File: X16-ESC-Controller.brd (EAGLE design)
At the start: 51.6 x 34.2 mm, 23 parts, among them J6 TMMH-110-05-F-D, U1 AZ1117IH-3.3TRG1

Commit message: 12/6/2023 pt2
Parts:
- renumbered JP1 to .., JP2 to .
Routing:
- net TIM1_CH2: track 46.4 -> 48.0 mm
- net GND: track 86.2 -> 84.9 mm
- net TIM3_CH2: track 49.6 -> 50.6 mm
- net TIM1_CH1: track 45.7 -> 46.3 mm
- net NRST: track 56.4 -> 57.0 mm
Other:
- board text added: "3V3"
- board text added: "NRST"
- board text added: "SWCLK"
- board text added: "SWDIO"

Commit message: 12/06/2023 pt3
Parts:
- D1, D2: device SparkFun-LED:LED-0603 -> SparkFun-LED:LED-0805
- moved D1 0.13 mm to (35.1, 27.6)
- moved D2 0.13 mm to (2.03, 9.14), turned to 270 degrees
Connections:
- removed net N$16: D2.A, R6.2
- new net N$1: D2.C, R6.2
- net 3V3: now also D2.A; no longer D2.C
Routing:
- net N$16: track 3.35 -> 0.00 mm
- net N$1: track 0.00 -> 3.31 mm
- net GND: track 84.9 -> 84.8 mm, vias 8 -> 26
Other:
- board text added: "5.2V"
- board text added: "Manya Kodi"
- board text added: "TIM1_CH1"
- board text added: "TIM1_CH2"
- board text added: "TIM1_CH3"
- board text added: "TIM1_CH4"
- board text added: "TIM2_CH1"
- board text added: "TIM2_CH2"
- board text added: "TIM2_CH3"
- board text added: "TIM2_CH4"
- board text added: "TIM3_CH1"
- board text added: "TIM3_CH2"
- board text added: "TIM3_CH3"
- board text added: "TIM3_CH4"
- board text added: "X16-ESC-CONTROLLER"
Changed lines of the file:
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@@
 <drawing>
 <settings>
-<setting alwaysvectorfont="no"/>
+<setting alwaysvectorfont="yes"/>
 <setting verticaltext="up"/>
 </settings>
@@
 <text x="46.609" y="29.337" size="0.508" layer="25">GND</text>
 <text x="46.482" y="32.004" size="0.508" layer="25">3V3</text>
+<text x="20.701" y="30.988" size="0.508" layer="25" rot="R90">TIM2_CH4</text>
+<text x="23.622" y="30.861" size="0.508" layer="25" rot="R90">TIM2_CH3</text>
+<text x="26.162" y="30.861" size="0.508" layer="25" rot="R90">TIM2_CH2</text>
+<text x="28.829" y="30.988" size="0.508" layer="25" rot="R90">TIM2_CH1</text>
+<text x="31.369" y="30.861" size="0.508" layer="25" rot="R90">TIM1_CH2</text>
+<text x="33.909" y="30.988" size="0.508" layer="25" rot="R90">TIM1_CH1</text>
+<text x="35.56" y="0.762" size="0.508" layer="25" rot="R90">TIM1_CH3</text>
+<text x="38.227" y="0.762" size="0.508" layer="25" rot="R90">TIM1_CH4</text>
+<text x="40.767" y="0.762" size="0.508" layer="25" rot="R90">TIM3_CH1</text>
+<text x="43.307" y="0.889" size="0.508" layer="25" rot="R90">TIM3_CH2</text>
+<text x="45.847" y="0.889" size="0.508" layer="25" rot="R90">TIM3_CH3</text>
+<text x="48.387" y="0.889" size="0.508" layer="25" rot="R90">TIM3_CH4</text>
+<text x="9.398" y="30.734" size="0.8128" layer="25" rot="R180">GND</text>
+<text x="9.144" y="23.368" size="0.8128" layer="25" rot="R180">3V3</text>
+<text x="13.208" y="3.302" size="0.8128" layer="25" rot="R180">5.2V</text>
+<text x="11.176" y="29.464" size="0.6096" layer="25">X16-ESC-CONTROLLER</text>
+<text x="11.938" y="28.321" size="0.6096" layer="25">Manya Kodi</text>
 </plain>
 <attributes>
@@
 <attribute name="VALUE" x="10.795" y="19.177" size="0.6096" layer="27" font="vector" ratio="20" rot="R90" align="top-center"/>
 </element>
-<element name="D1" library="SparkFun-LED" library_urn="urn:adsk.eagle:library:529" package="LED-0603" package3d_urn="urn:adsk.eagle:package:39354/2" value="Green" x="35.179" y="27.559" smashed="yes" rot="R180">
-<attribute name="NAME" x="35.179" y="26.924" size="0.6096" layer="25" font="vector" ratio="20" rot="R180" align="bottom-center"/>
-<attribute name="PROD_ID" value="DIO-16512" x="-10.541" y="74.549" size="1.778" layer="27" rot="R180" display="off"/>
-<attribute name="VALUE" x="35.179" y="28.194" size="0.6096" layer="27" font="vector" ratio="20" rot="R180" align="top-center"/>
-</element>
-<element name="D2" library="SparkFun-LED" library_urn="urn:adsk.eagle:library:529" package="LED-0603" package3d_urn="urn:adsk.eagle:package:39354/2" value="Green" x="2.032" y="9.017" smashed="yes" rot="R90">
-<attribute name="NAME" x="1.397" y="9.017" size="0.6096" layer="25" font="vector" ratio="20" rot="R90" align="bottom-center"/>
-<attribute name="PROD_ID" value="DIO-16512" x="49.022" y="58.547" size="1.778" layer="27" rot="R90" display="off"/>
-<attribute name="VALUE" x="2.667" y="9.017" size="0.6096" layer="27" font="vector" ratio="20" rot="R90" align="top-center"/>
+<element name="D1" library="SparkFun-LED" library_urn="urn:adsk.eagle:library:529" package="LED-0805" package3d_urn="urn:adsk.eagle:package:41389318/1" value="Green" x="35.052" y="27.559" smashed="yes" rot="R180">
+<attribute name="NAME" x="35.052" y="26.924" size="0.6096" layer="25" font="vector" ratio="20" rot="R180" align="bottom-center"/>
+</element>
+<element name="D2" library="SparkFun-LED" library_urn="urn:adsk.eagle:library:529" package="LED-0805" package3d_urn="urn:adsk.eagle:package:41389318/1" value="Green" x="2.032" y="9.144" smashed="yes" rot="R270">
+<attribute name="NAME" x="2.667" y="9.144" size="0.6096" layer="25" font="vector" ratio="20" rot="R270" align="bottom-center"/>
 </element>
 <element name="J1" library="SparkFun-Connectors" library_urn="urn:adsk.eagle:library:513" package="1X06_NO_SILK" package3d_urn="urn:adsk.eagle:package:38130/2" value="" x="34.798" y="32.385" smashed="yes" rot="R180">
@@
 <wire x1="33.528" y1="19.343" x2="31.242" y2="19.343" width="0.2032" layer="16"/>
 <wire x1="31.168" y1="22.544" x2="31.968" y2="22.544" width="0.2032" layer="1"/>
-<wire x1="31.968" y1="25.225" x2="34.302" y2="27.559" width="0.2032" layer="1"/>
-<wire x1="31.968" y1="22.544" x2="31.968" y2="25.225" width="0.2032" layer="1"/>
+<wire x1="31.968" y1="25.362165625" x2="34.002" y2="27.559" width="0.2032" layer="1"/>
+<wire x1="31.968" y1="22.544" x2="31.968" y2="25.362165625" width="0.2032" layer="1"/>
 <via x="31.877" y="17.907" extent="1-16" drill="0.35"/>
 <wire x1="35.648" y1="14.898" x2="36.576" y2="14.898" width="0.2032" layer="1"/>
@@
 <wire x1="43.561" y1="12.7" x2="43.942" y2="12.319" width="0.2032" layer="16"/>
 <wire x1="43.942" y1="12.319" x2="43.942" y2="6.985" width="0.2032" layer="16"/>
+<via x="9.398" y="32.004" extent="1-16" drill="0.35"/>
+<via x="4.826" y="15.367" extent="1-16" drill="0.35"/>
+<via x="4.953" y="11.43" extent="1-16" drill="0.35"/>
+<via x="4.953" y="7.239" extent="1-16" drill="0.35"/>
+<via x="12.446" y="13.843" extent="1-16" drill="0.35"/>
+<via x="12.446" y="10.16" extent="1-16" drill="0.35"/>
+<via x="12.573" y="6.35" extent="1-16" drill="0.35"/>
+<via x="9.652" y="28.702" extent="1-16" drill="0.35"/>
+<via x="9.652" y="25.019" extent="1-16" drill="0.35"/>
+<via x="14.351" y="25.019" extent="1-16" drill="0.35"/>
+<via x="18.669" y="25.019" extent="1-16" drill="0.35"/>
+<via x="38.227" y="32.004" extent="1-16" drill="0.35"/>
+<via x="41.656" y="32.004" extent="1-16" drill="0.35"/>
+<via x="45.212" y="32.004" extent="1-16" drill="0.35"/>
+<via x="45.466" y="27.686" extent="1-16" drill="0.35"/>
+<via x="43.561" y="30.099" extent="1-16" drill="0.35"/>
+<via x="30.099" y="26.543" extent="1-16" drill="0.35"/>
+<via x="46.609" y="20.193" extent="1-16" drill="0.35"/>
 </signal>
 <signal name="TIM2_CH1">
@@
 <wire x1="35.4076" y1="1.3716" x2="30.353" y2="1.3716" width="0.2032" layer="16"/>
 <wire x1="30.353" y1="1.3716" x2="29.819021875" y2="1.905578125" width="0.2032" layer="16"/>
-<wire x1="29.819021875" y1="3.532021875" x2="30.859" y2="4.572" width="0.2032" layer="16"/>
-<wire x1="29.819021875" y1="1.905578125" x2="29.819021875" y2="3.532021875" width="0.2032" layer="16"/>
+<wire x1="30.859" y1="4.191" x2="29.819021875" y2="3.151021875" width="0.2032" layer="16"/>
+<wire x1="30.859" y1="4.191" x2="30.859" y2="4.572" width="0.2032" layer="16"/>
+<wire x1="29.819021875" y1="1.905578125" x2="29.819021875" y2="3.151021875" width="0.2032" layer="16"/>
 <wire x1="40.8714" y1="7.62" x2="40.894" y2="7.6426" width="0.2032" layer="1"/>
 <wire x1="40.894" y1="16.891" x2="40.894" y2="7.6426" width="0.2032" layer="1"/>
@@
 <contactref element="R2" pad="2"/>
 <contactref element="D1" pad="A"/>
-<wire x1="36.056" y1="27.559" x2="36.056" y2="25.808" width="0.2032" layer="1"/>
-<wire x1="36.056" y1="25.808" x2="36.029" y2="25.781" width="0.2032" layer="1"/>
+<wire x1="36.029" y1="25.781" x2="36.029" y2="26.8201375" width="0.2032" layer="1"/>
+<wire x1="36.102" y1="27.559" x2="36.029" y2="26.8201375" width="0.2032" layer="1"/>
 </signal>
 <signal name="MISO">
@@
 <wire x1="18.859" y1="14.922" x2="18.859" y2="4.572" width="0.2032" layer="16"/>
 <wire x1="19.4338" y1="15.4968" x2="18.859" y2="14.922" width="0.2032" layer="16"/>
-</signal>
-<signal name="N$16">
-<contactref element="R6" pad="2"/>
-<contactref element="D2" pad="A"/>
-<wire x1="2.032" y1="8.14" x2="2.032" y2="4.787" width="0.2032" layer="1"/>
 </signal>
 <signal name="MOSI">
@@
 <contactref element="U1" pad="2"/>
 <contactref element="C7" pad="1"/>
-<contactref element="D2" pad="C"/>
 <wire x1="33.528" y1="21.043" x2="31.242" y2="21.043" width="0.508" layer="16"/>
 <wire x1="31.242" y1="21.043" x2="28.36" y2="21.043" width="0.508" layer="16"/>
@@
 <wire x1="4.318" y1="22.606" x2="4.064" y2="22.86" width="0.508" layer="1"/>
 <wire x1="4.318" y1="22.606" x2="4.318" y2="18.454" width="0.508" layer="1"/>
-<wire x1="2.032" y1="9.894" x2="2.032" y2="16.168" width="0.508" layer="1"/>
-<wire x1="2.032" y1="16.168" x2="4.191" y2="18.327" width="0.508" layer="1"/>
+<wire x1="2.032" y1="16.168" x2="2.1395" y2="16.2755" width="0.508" layer="1"/>
+<wire x1="2.0125" y1="16.1485" x2="2.032" y2="16.168" width="0.508" layer="1"/>
+<wire x1="2.1395" y1="16.2755" x2="4.191" y2="18.327" width="0.508" layer="1"/>
 <wire x1="4.191" y1="18.327" x2="4.318" y2="18.454" width="0.508" layer="1"/>
 <contactref element="R1" pad="2"/>
@@
 <wire x1="27.686" y1="20.447" x2="28.321" y2="21.082" width="0.508" layer="1"/>
 <wire x1="27.686" y1="20.447" x2="27.686" y2="18.288" width="0.508" layer="1"/>
+<contactref element="D2" pad="A"/>
+<wire x1="2.0125" y1="16.1485" x2="2.0125" y2="10.2135" width="0.508" layer="1"/>
+<wire x1="2.032" y1="10.194" x2="2.0125" y2="10.2135" width="0.508" layer="1"/>
 </signal>
 <signal name="5.2V">
@@
 <wire x1="32.766" y1="14.042" x2="32.768" y2="14.044" width="0.2032" layer="1"/>
 </signal>
+<signal name="N$1">
+<contactref element="R6" pad="2"/>
+<contactref element="D2" pad="C"/>
+<wire x1="2.032" y1="8.094" x2="2.032" y2="4.787" width="0.508" layer="1"/>
+</signal>
 </signals>

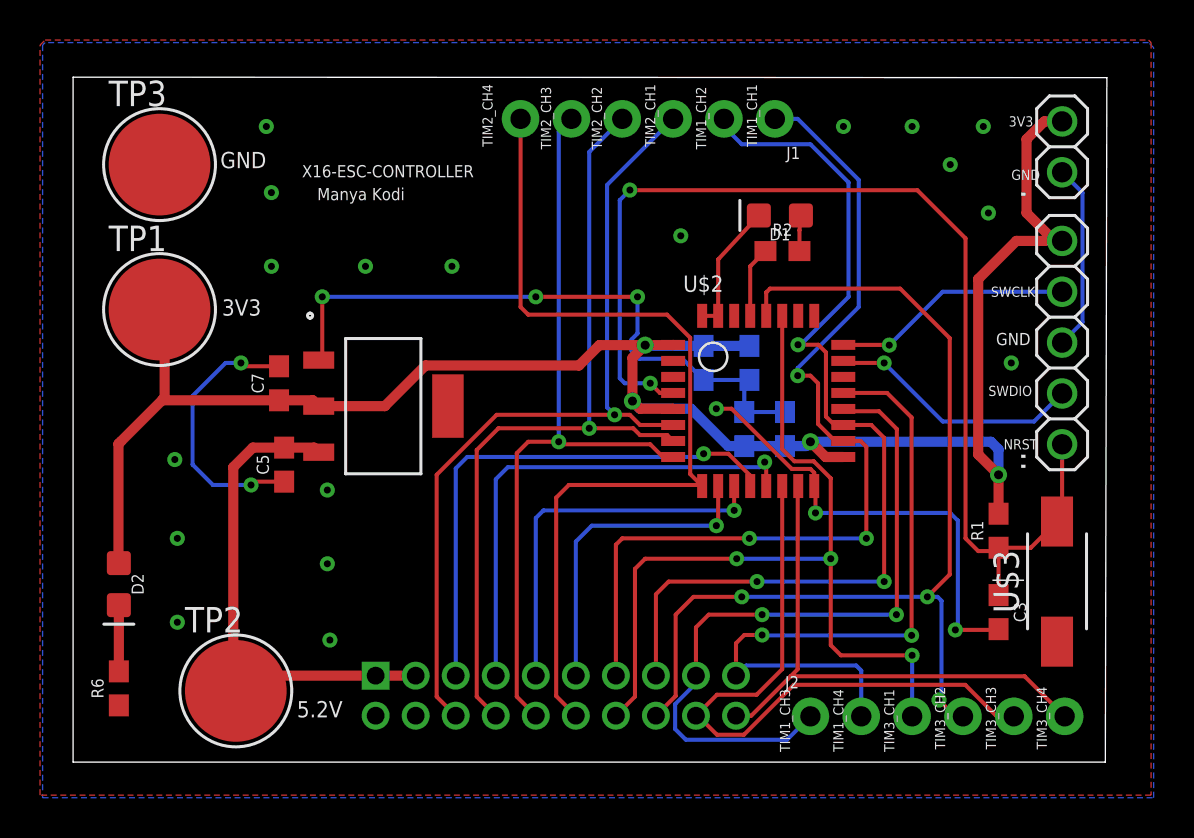
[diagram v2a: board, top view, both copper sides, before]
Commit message: increased text size + minor changes to trace routing
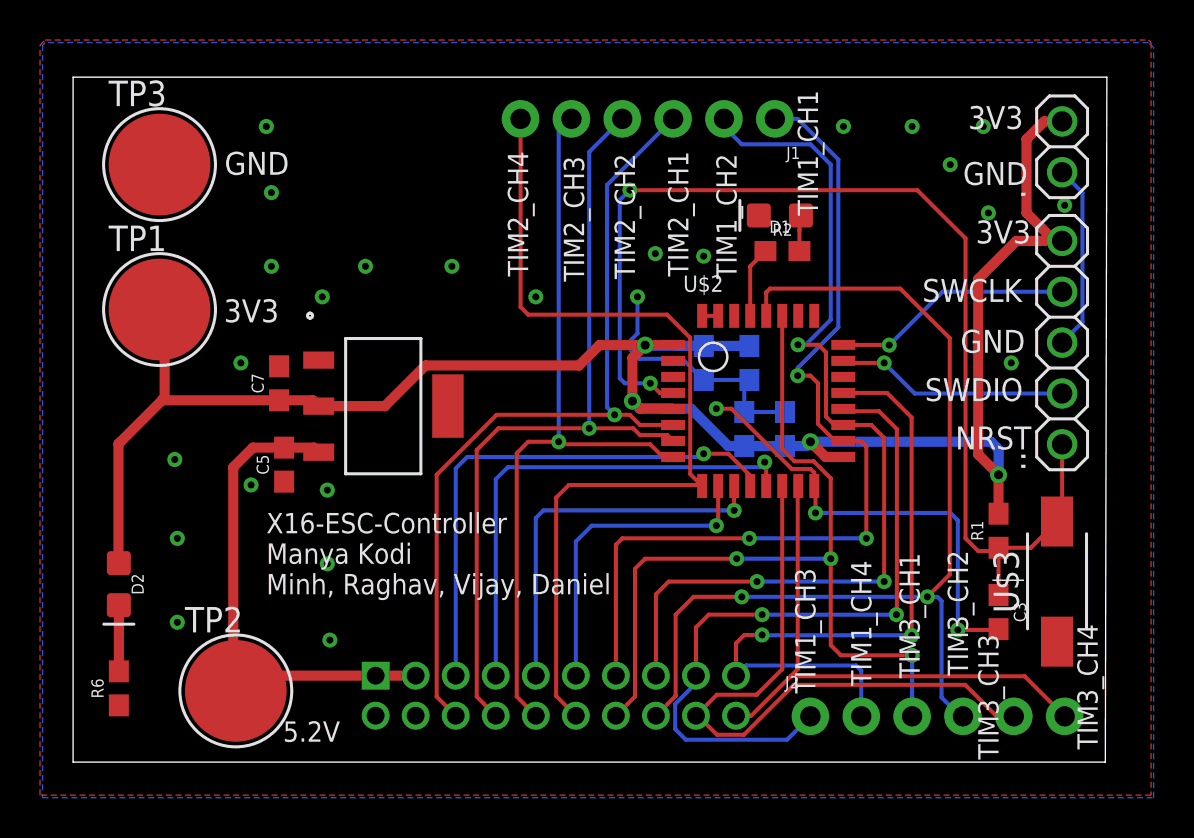
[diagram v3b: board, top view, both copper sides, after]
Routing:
- net GND: track 84.8 -> 46.5 mm, vias 26 -> 28
- net SWDIO: track 12.8 -> 11.6 mm
- net TIM1_CH1: track 46.3 -> 45.5 mm
- net TIM1_CH2: track 48.0 -> 47.4 mm
- net TIM3_CH2: track 50.6 -> 50.3 mm, vias 3 -> 2
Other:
- board text added: "X16-ESC-Controller Manya Kodi Minh, Raghav, Vijay, Daniel"
- board text removed: "Manya Kodi"
- board text removed: "X16-ESC-CONTROLLER"

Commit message: fixed LDO thermals and pad 4, updated LDO caps to datasheet recommended, cleaned up silkscreen
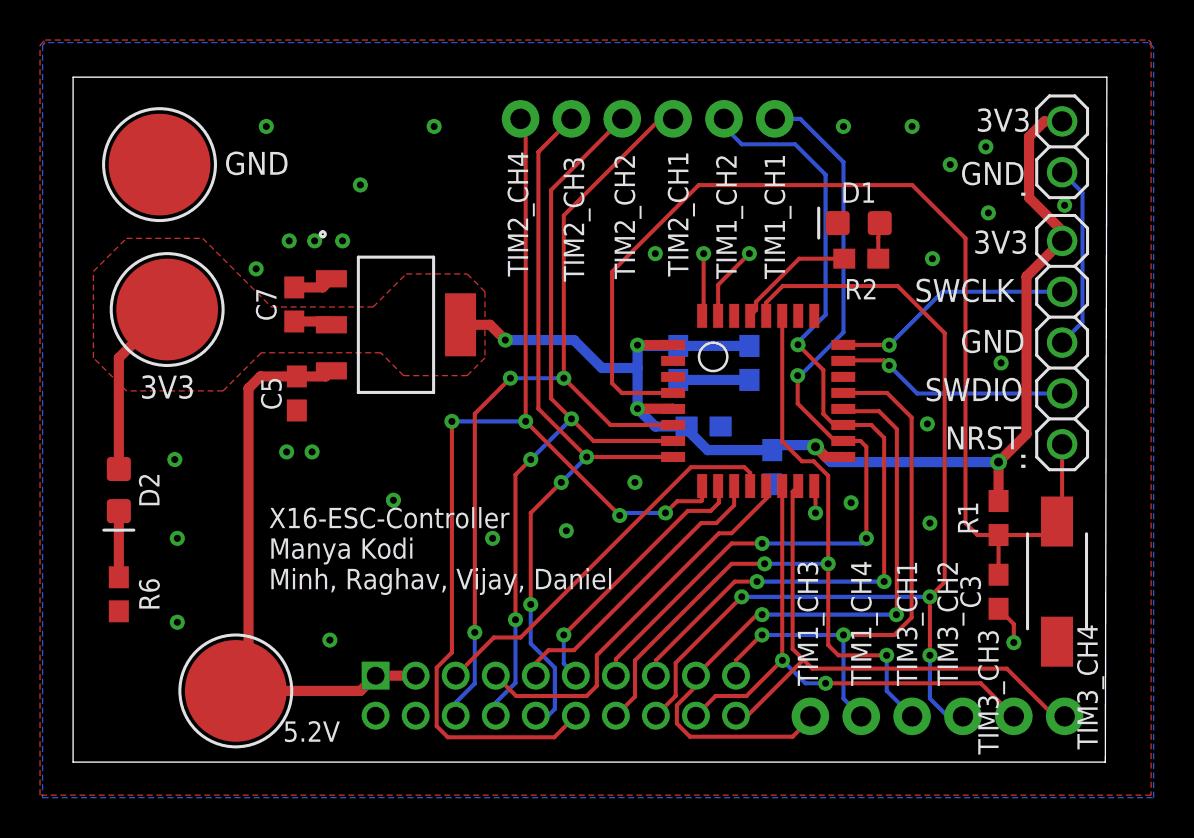
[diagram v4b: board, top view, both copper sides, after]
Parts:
- C5: value 4.7uF -> 10uF
- C7: value 4.7uF -> 22uF
- moved D2 4.70 mm to (2.03, 13.8)
- moved R6 4.70 mm to (2.03, 8.64)
- moved U1 4.11 mm to (15.9, 22.1)
- moved C7 4.01 mm to (10.8, 23.1)
- moved D1 3.96 mm to (39.0, 27.2)
- moved R2 3.96 mm to (39.1, 25.4)
- moved C5 3.61 mm to (10.9, 18.7)
- moved C2 2.04 mm to (31.2, 17.0), turned to 180 degrees
- moved C6 2.01 mm to (34.7, 15.0), turned to 270 degrees
- moved C1 1.27 mm to (30.0, 20.2)
- moved C3 1.02 mm to (46.0, 8.76)
- moved R1 0.63 mm to (46.0, 12.4)
- moved TP1 0.38 mm to (4.45, 22.9)
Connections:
- net 3V3: now also U1.4
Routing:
- net 3V3: track 99.1 -> 76.2 mm, vias 4 -> 5
- net GND: track 46.5 -> 25.2 mm, vias 28 -> 33
- net TIM2_CH4: track 45.0 -> 53.9 mm, vias 0 -> 4
- net MISO: track 26.3 -> 19.8 mm, vias 1 -> 0
- net TIM1_CH4: track 34.2 -> 28.8 mm
- net TIM3_CH3: track 32.3 -> 26.9 mm, vias 0 -> 2
- net MOSI: track 24.8 -> 19.6 mm, vias 1 -> 0
- net SCLK: track 19.2 -> 14.8 mm, vias 1 -> 0
- net 5.2V: track 25.0 -> 29.2 mm
- net TIM3_CH1: track 43.1 -> 39.3 mm
- net TIM1_CH2: track 47.4 -> 44.0 mm
- net TIM1_CH1: track 45.5 -> 42.1 mm
- net N$3: track 3.55 -> 6.12 mm
- net CS: track 16.1 -> 13.6 mm
- net NRST: track 57.0 -> 54.6 mm, vias 2 -> 0
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- added copper zone on layer 1, net 3V3

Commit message: Minh Update 1
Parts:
- moved TP1 0.30 mm to (4.19, 22.7)
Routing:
- net 3V3: track 76.2 -> 72.7 mm
- net GND: vias 33 -> 29
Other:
- board text added: "T1C1"
- board text added: "T1C2"
- board text added: "T1C3"
- board text added: "T1C4"
- board text added: "T2C1"
- board text added: "T2C2"
- board text added: "T2C3"
- board text added: "T2C4"
- board text added: "T3C1"
- board text added: "T3C2"
- board text added: "T3C3"
- board text added: "T3C4"
- board text added: "U$2"
- board text removed: "TIM1_CH1"
- board text removed: "TIM1_CH2"
- board text removed: "TIM1_CH3"
- board text removed: "TIM1_CH4"
- board text removed: "TIM2_CH1"
- board text removed: "TIM2_CH2"
- board text removed: "TIM2_CH3"
- board text removed: "TIM2_CH4"
- board text removed: "TIM3_CH1"
- board text removed: "TIM3_CH2"
- board text removed: "TIM3_CH3"
- board text removed: "TIM3_CH4"
